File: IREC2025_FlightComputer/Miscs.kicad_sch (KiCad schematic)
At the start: 14 parts, among them U7 THGBMUG6C1LBAIL

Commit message: small fixes
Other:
- moved on the sheet: C73, R49, R50, R51, R52, R53, R54, R55, R56, R57, R58, U7

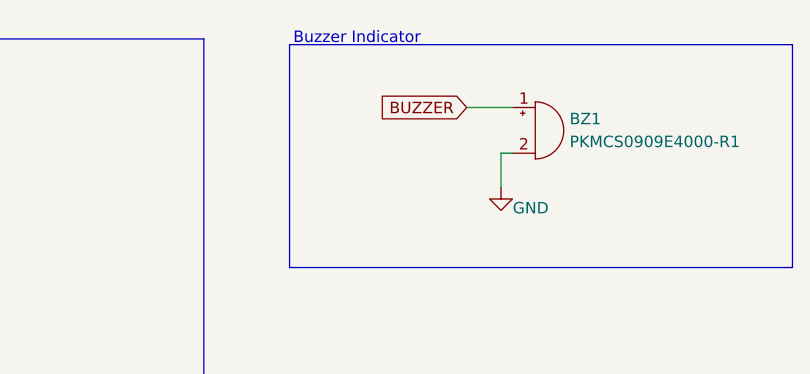
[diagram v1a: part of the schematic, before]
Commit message: Added silkscreen + Layout Minorchange
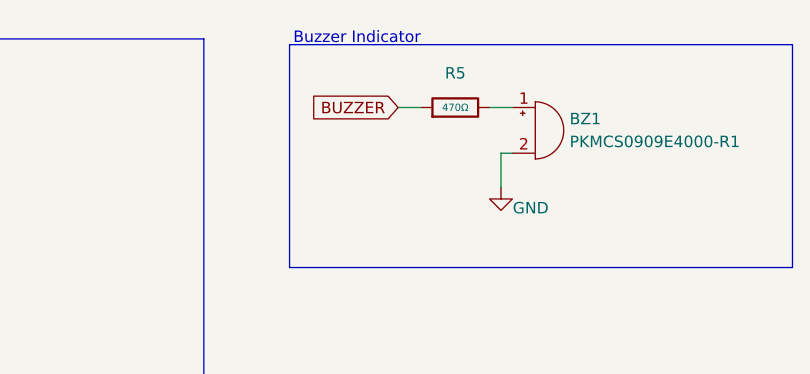
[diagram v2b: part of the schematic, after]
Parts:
- added R5: 470Ω, PCM_JLCPCB:R_0402, symbol PCM_JLCPCB-Resistors:0402,470Ω
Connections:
- net BUZZER: now also R5.1; no longer BZ1.1 (+)
- new net: BZ1.1 (+), R5.2
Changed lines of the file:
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@@
 	(wire
 		(pts
-			(xy 181.61 35.56) (xy 186.69 35.56)
-		)
-		(stroke
-			(width 0)
-			(type default)
-		)
-	)
-	(wire
-		(pts
 			(xy 100.33 209.55) (xy 115.57 209.55)
 		)
@@
 	(wire
 		(pts
+			(xy 173.99 35.56) (xy 176.53 35.56)
+		)
+		(stroke
+			(width 0)
+			(type default)
+		)
+	)
+	(wire
+		(pts
 			(xy 115.57 113.03) (xy 115.57 181.61)
 		)
@@
 	(wire
 		(pts
+			(xy 184.15 35.56) (xy 186.69 35.56)
+		)
+		(stroke
+			(width 0)
+			(type default)
+		)
+	)
+	(wire
+		(pts
 			(xy 111.76 179.07) (xy 111.76 207.01)
 		)
@@
 	(global_label "BUZZER"
 		(shape input)
-		(at 181.61 35.56 180)
+		(at 173.99 35.56 180)
 		(fields_autoplaced yes)
 		(effects
@@
 		)
 		(property "Intersheetrefs" "${INTERSHEET_REFS}"
-			(at 171.1863 35.56 0)
+			(at 163.5663 35.56 0)
 			(effects
 				(font
@@
 					(unit 1)
 				)
+			)
+		)
+	)
+	(symbol
+		(lib_id "PCM_JLCPCB-Resistors:0402,470Ω")
+		(at 180.34 35.56 90)
+		(unit 1)
+		(exclude_from_sim no)
+		(in_bom yes)
+		(on_board yes)
+		(dnp no)
+		(fields_autoplaced yes)
+		(property "Reference" "R5"
+			(at 180.34 31.75 90)
+			(effects
+				(font
+					(size 1.27 1.27)
+				)
+			)
+		)
+		(property "Value" "470Ω"
+			(at 180.34 35.56 90)
+			(do_not_autoplace yes)
+			(effects
+				(font
+					(size 0.8 0.8)
+				)
+			)
+		)
+		(property "Footprint" "PCM_JLCPCB:R_0402"
+			(at 180.34 37.338 90)
+			(effects
+				(font
+					(size 1.27 1.27)
+				)
+				(hide yes)
+			)
+		)
+		(property "Datasheet" "https://www.lcsc.com/datasheet/lcsc_datasheet_2205311900_UNI-ROYAL-Uniroyal-Elec-0402WGF4700TCE_C25117.pdf"
+			(at 180.34 35.56 0)
+			(effects
+				(font
+					(size 1.27 1.27)
+				)
+				(hide yes)
+			)
+		)
+		(property "Description" "62.5mW Thick Film Resistors 50V ±100ppm/°C ±1% 470Ω 0402 Chip Resistor - Surface Mount ROHS"
+			(at 180.34 35.56 0)
+			(effects
+				(font
+					(size 1.27 1.27)
+				)
+				(hide yes)
+			)
+		)
+		(property "LCSC" "C25117"
+			(at 180.34 35.56 0)
+			(effects
+				(font
+					(size 1.27 1.27)
+				)
+				(hide yes)
+			)
+		)
+		(property "Stock" "591787"
+			(at 180.34 35.56 0)
+			(effects
+				(font
+					(size 1.27 1.27)
+				)
+				(hide yes)
+			)
+		)
+		(property "Price" "0.004USD"
+			(at 180.34 35.56 0)
+			(effects
+				(font
+					(size 1.27 1.27)
+				)
+				(hide yes)
+			)
+		)
+		(property "Process" "SMT"
+			(at 180.34 35.56 0)
+			(effects
+				(font
+					(size 1.27 1.27)
+				)
+				(hide yes)
+			)
+		)
+		(property "Minimum Qty" "20"
+			(at 180.34 35.56 0)
+			(effects
+				(font
+					(size 1.27 1.27)
+				)
+				(hide yes)
+			)
+		)
+		(property "Attrition Qty" "10"
+			(at 180.34 35.56 0)
+			(effects
+				(font
+					(size 1.27 1.27)
+				)
+				(hide yes)
+			)
+		)
+		(property "Class" "Basic Component"
+			(at 180.34 35.56 0)
+			(effects
+				(font
+					(size 1.27 1.27)
+				)
+				(hide yes)
+			)
+		)
+		(property "Category" "Resistors,Chip Resistor - Surface Mount"
+			(at 180.34 35.56 0)
+			(effects
+				(font
+					(size 1.27 1.27)
+				)
+				(hide yes)
+			)
+		)
+		(property "Manufacturer" "UNI-ROYAL(Uniroyal Elec)"
+			(at 180.34 35.56 0)
+			(effects
+				(font
+					(size 1.27 1.27)
+				)
+				(hide yes)
+			)
+		)
+		(property "Part" "0402WGF4700TCE"
+			(at 180.34 35.56 0)
+			(effects
+				(font
+					(size 1.27 1.27)
+				)
+				(hide yes)
+			)
+		)
+		(property "Resistance" "470Ω"
+			(at 180.34 35.56 0)
+			(effects
+				(font
+					(size 1.27 1.27)
+				)
+				(hide yes)
+			)
+		)
+		(property "Power(Watts)" "62.5mW"
+			(at 180.34 35.56 0)
+			(effects
+				(font
+					(size 1.27 1.27)
+				)
+				(hide yes)
+			)
+		)
+		(property "Type" "Thick Film Resistors"
+			(at 180.34 35.56 0)
+			(effects
+				(font
+					(size 1.27 1.27)
+				)
+				(hide yes)
+			)
+		)
+		(property "Overload Voltage (Max)" "50V"
+			(at 180.34 35.56 0)
+			(effects
+				(font
+					(size 1.27 1.27)
+				)
+				(hide yes)
+			)
+		)
+		(property "Operating Temperature Range" "-55°C~+155°C"
+			(at 180.34 35.56 0)
+			(effects
+				(font
+					(size 1.27 1.27)
+				)
+				(hide yes)
+			)
+		)
+		(property "Tolerance" "±1%"
+			(at 180.34 35.56 0)
+			(effects
+				(font
+					(size 1.27 1.27)
+				)
+				(hide yes)
+			)
+		)
+		(property "Temperature Coefficient" "±100ppm/°C"
+			(at 180.34 35.56 0)
+			(effects
+				(font
+					(size 1.27 1.27)
+				)
+				(hide yes)
+			)
+		)
+		(pin "1"
+		)
+		(pin "2"
+		)
+		(instances
+			(project ""
+				(path "/d402aac1-6798-4745-a2ce-fc3f8e4c9afb/e5fd5176-e33b-4137-b737-1b6a7c4448a9"
+					(reference "R5")
+					(unit 1)
+				)

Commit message: 2 designs
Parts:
- renumbered BZ1 to BZ?, R5 to R?, U6 to U?
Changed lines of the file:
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@@
 		(dnp no)
 		(fields_autoplaced yes)
-		(property "Reference" "BZ1"
+		(property "Reference" "BZ?"
 			(at 193.04 36.8299 0)
 			(effects
@@
 		)
 		(instances
-			(project ""
+			(project "IREC2025_FlightComputer"
 				(path "/d402aac1-6798-4745-a2ce-fc3f8e4c9afb/e5fd5176-e33b-4137-b737-1b6a7c4448a9"
-					(reference "BZ1")
+					(reference "BZ?")
 					(unit 1)
 				)
@@
 		(dnp no)
 		(fields_autoplaced yes)
-		(property "Reference" "R5"
+		(property "Reference" "R?"
 			(at 180.34 31.75 90)
 			(effects
@@
 		)
 		(instances
-			(project ""
+			(project "IREC2025_FlightComputer"
 				(path "/d402aac1-6798-4745-a2ce-fc3f8e4c9afb/e5fd5176-e33b-4137-b737-1b6a7c4448a9"
-					(reference "R5")
+					(reference "R?")
 					(unit 1)
 				)
@@
 		(dnp no)
 		(fields_autoplaced yes)
-		(property "Reference" "U6"
+		(property "Reference" "U?"
 			(at 204.47 75.5649 0)
 			(effects
@@
 		)
 		(instances
-			(project ""
+			(project "IREC2025_FlightComputer"
 				(path "/d402aac1-6798-4745-a2ce-fc3f8e4c9afb/e5fd5176-e33b-4137-b737-1b6a7c4448a9"
-					(reference "U6")
+					(reference "U?")
 					(unit 1)
 				)

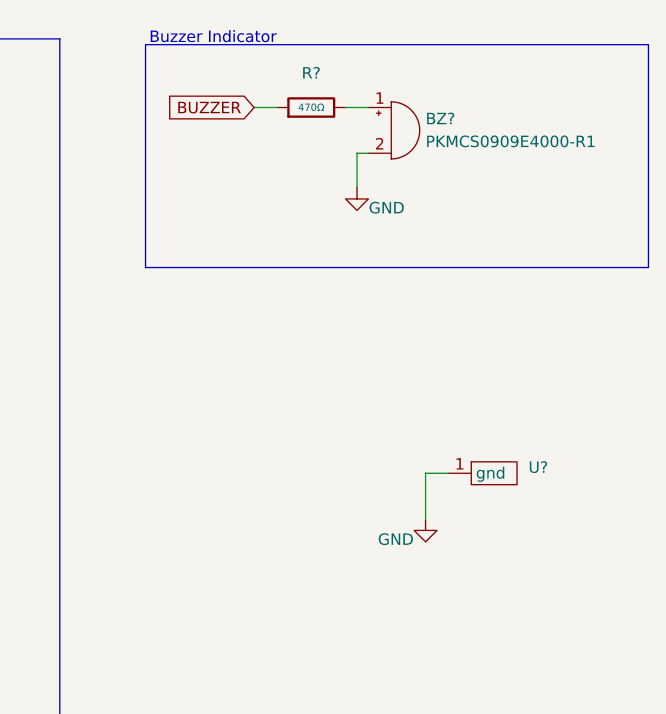
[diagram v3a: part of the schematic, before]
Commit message: changed most resistors to 0603
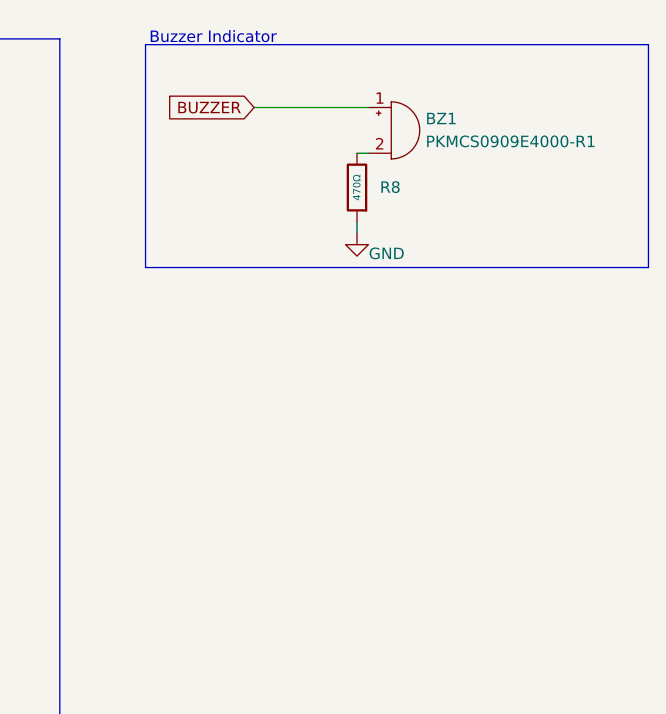
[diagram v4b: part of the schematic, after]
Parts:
- removed U?: ~, RFshielddd:MS233-20, symbol shieldrf:shieldrff
- R8: renamed from R?; footprint PCM_JLCPCB:R_0402 -> PCM_JLCPCB:R_0603
- gave numbers to parts that had none: 1
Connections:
- net BUZZER: now also BZ1.1 (+); no longer R8.1
- net GND: now also R8.1; no longer BZ1.2 (-)
- net at R8.2: now also BZ1.2 (-); no longer BZ1.1 (+)
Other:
- moved on the sheet: R8
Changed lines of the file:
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@@
 	(wire
 		(pts
-			(xy 193.04 81.28) (xy 193.04 76.2)
-		)
-		(stroke
-			(width 0)
-			(type default)
-		)
-	)
-	(wire
-		(pts
 			(xy 72.39 82.55) (xy 72.39 95.25)
 		)
@@
 	(wire
 		(pts
-			(xy 185.42 44.45) (xy 185.42 40.64)
-		)
-		(stroke
-			(width 0)
-			(type default)
-		)
-	)
-	(wire
-		(pts
 			(xy 100.33 209.55) (xy 115.57 209.55)
 		)
@@
 	(wire
 		(pts
-			(xy 193.04 76.2) (xy 195.58 76.2)
-		)
-		(stroke
-			(width 0)
-			(type default)
-		)
-	)
-	(wire
-		(pts
 			(xy 67.31 92.71) (xy 77.47 92.71)
 		)
@@
 	(wire
 		(pts
-			(xy 173.99 35.56) (xy 176.53 35.56)
-		)
-		(stroke
-			(width 0)
-			(type default)
-		)
-	)
-	(wire
-		(pts
 			(xy 115.57 113.03) (xy 115.57 181.61)
 		)
@@
 	(wire
 		(pts
-			(xy 184.15 35.56) (xy 186.69 35.56)
-		)
-		(stroke
-			(width 0)
-			(type default)
-		)
-	)
-	(wire
-		(pts
 			(xy 111.76 179.07) (xy 111.76 207.01)
 		)
@@
 	(wire
 		(pts
+			(xy 185.42 48.26) (xy 185.42 49.53)
+		)
+		(stroke
+			(width 0)
+			(type default)
+		)
+	)
+	(wire
+		(pts
 			(xy 77.47 125.73) (xy 67.31 125.73)
 		)
@@
 	(wire
 		(pts
+			(xy 173.99 35.56) (xy 186.69 35.56)
+		)
+		(stroke
+			(width 0)
+			(type default)
+		)
+	)
+	(wire
+		(pts
 			(xy 100.33 113.03) (xy 115.57 113.03)
 		)
@@
 		(dnp no)
 		(fields_autoplaced yes)
-		(property "Reference" "BZ?"
+		(property "Reference" "BZ1"
 			(at 193.04 36.8299 0)
 			(effects
@@
 			(project "IREC2025_FlightComputer"
 				(path "/d402aac1-6798-4745-a2ce-fc3f8e4c9afb/e5fd5176-e33b-4137-b737-1b6a7c4448a9"
-					(reference "BZ?")
+					(reference "BZ1")
 					(unit 1)
 				)
@@
 	(symbol
 		(lib_id "PCM_JLCPCB-Resistors:0402,470Ω")
-		(at 180.34 35.56 90)
+		(at 185.42 44.45 180)
 		(unit 1)
 		(exclude_from_sim no)
@@
 		(dnp no)
 		(fields_autoplaced yes)
-		(property "Reference" "R?"
-			(at 180.34 31.75 90)
+		(property "Reference" "R8"
+			(at 187.96 44.4499 0)
 			(effects
 				(font
 					(size 1.27 1.27)
 				)
+				(justify right)
 			)
 		)
 		(property "Value" "470Ω"
-			(at 180.34 35.56 90)
+			(at 185.42 44.45 90)
 			(do_not_autoplace yes)
 			(effects
@@
 			)
 		)
-		(property "Footprint" "PCM_JLCPCB:R_0402"
-			(at 180.34 37.338 90)
+		(property "Footprint" "PCM_JLCPCB:R_0603"
+			(at 187.198 44.45 90)
 			(effects
 				(font
@@
 		)
 		(property "Datasheet" "https://www.lcsc.com/datasheet/lcsc_datasheet_2205311900_UNI-ROYAL-Uniroyal-Elec-0402WGF4700TCE_C25117.pdf"
-			(at 180.34 35.56 0)
+			(at 185.42 44.45 0)
 			(effects
 				(font
@@
 		)
 		(property "Description" "62.5mW Thick Film Resistors 50V ±100ppm/°C ±1% 470Ω 0402 Chip Resistor - Surface Mount ROHS"
-			(at 180.34 35.56 0)
+			(at 185.42 44.45 0)
 			(effects
 				(font
@@
 		)
 		(property "LCSC" "C25117"
-			(at 180.34 35.56 0)
+			(at 185.42 44.45 0)
 			(effects
 				(font
@@
 		)
 		(property "Stock" "591787"
-			(at 180.34 35.56 0)
+			(at 185.42 44.45 0)
 			(effects
 				(font
@@
 		)
 		(property "Price" "0.004USD"
-			(at 180.34 35.56 0)
+			(at 185.42 44.45 0)
 			(effects
 				(font
@@
 		)
 		(property "Process" "SMT"
-			(at 180.34 35.56 0)
+			(at 185.42 44.45 0)
 			(effects
 				(font
@@
 		)
 		(property "Minimum Qty" "20"
-			(at 180.34 35.56 0)
+			(at 185.42 44.45 0)
 			(effects
 				(font
@@
 		)
 		(property "Attrition Qty" "10"
-			(at 180.34 35.56 0)
+			(at 185.42 44.45 0)
 			(effects
 				(font
@@
 		)
 		(property "Class" "Basic Component"
-			(at 180.34 35.56 0)
+			(at 185.42 44.45 0)
 			(effects
 				(font
@@
 		)
 		(property "Category" "Resistors,Chip Resistor - Surface Mount"
-			(at 180.34 35.56 0)
+			(at 185.42 44.45 0)
 			(effects
 				(font
@@
 		)
 		(property "Manufacturer" "UNI-ROYAL(Uniroyal Elec)"
-			(at 180.34 35.56 0)
+			(at 185.42 44.45 0)
 			(effects
 				(font
@@
 		)
 		(property "Part" "0402WGF4700TCE"
-			(at 180.34 35.56 0)
+			(at 185.42 44.45 0)
 			(effects
 				(font
@@
 		)
 		(property "Resistance" "470Ω"
-			(at 180.34 35.56 0)
+			(at 185.42 44.45 0)
 			(effects
 				(font
@@
 		)
 		(property "Power(Watts)" "62.5mW"
-			(at 180.34 35.56 0)
+			(at 185.42 44.45 0)
 			(effects
 				(font
@@
 		)
 		(property "Type" "Thick Film Resistors"
-			(at 180.34 35.56 0)
+			(at 185.42 44.45 0)
 			(effects
 				(font
@@
 		)
 		(property "Overload Voltage (Max)" "50V"
-			(at 180.34 35.56 0)
+			(at 185.42 44.45 0)
 			(effects
 				(font
@@
 		)
 		(property "Operating Temperature Range" "-55°C~+155°C"
-			(at 180.34 35.56 0)
+			(at 185.42 44.45 0)
 			(effects
 				(font
@@
 		)
 		(property "Tolerance" "±1%"
-			(at 180.34 35.56 0)
+			(at 185.42 44.45 0)
 			(effects
 				(font
@@
 		)
 		(property "Temperature Coefficient" "±100ppm/°C"
-			(at 180.34 35.56 0)
+			(at 185.42 44.45 0)
 			(effects
 				(font
@@
 			(project "IREC2025_FlightComputer"
 				(path "/d402aac1-6798-4745-a2ce-fc3f8e4c9afb/e5fd5176-e33b-4137-b737-1b6a7c4448a9"
-					(reference "R?")
+					(reference "R8")
 					(unit 1)
 				)
@@
 	(symbol
 		(lib_id "power:GND")
-		(at 193.04 81.28 0)
-		(unit 1)
-		(exclude_from_sim no)
-		(in_bom yes)
-		(on_board yes)
-		(dnp no)
-		(property "Reference" "#PWR0118"
-			(at 193.04 87.63 0)
-			(effects
-				(font
-					(size 1.27 1.27)
-				)
-				(hide yes)
-			)
-		)
-		(property "Value" "GND"
-			(at 189.738 83.566 0)
-			(effects
-				(font
-					(size 1.27 1.27)
-				)
-			)
-		)
-		(property "Footprint" ""
-			(at 193.04 81.28 0)
-			(effects
-				(font
-					(size 1.27 1.27)
-				)
-				(hide yes)
-			)
-		)
-		(property "Datasheet" ""
-			(at 193.04 81.28 0)
-			(effects
-				(font
-					(size 1.27 1.27)
-				)
-				(hide yes)
-			)
-		)
-		(property "Description" "Power symbol creates a global label with name \"GND\" , ground"
-			(at 193.04 81.28 0)
-			(effects
-				(font
-					(size 1.27 1.27)
-				)
-				(hide yes)
-			)
-		)
-		(pin "1"
-		)
-		(instances
-			(project "IREC2025_FlightComputer"
-				(path "/d402aac1-6798-4745-a2ce-fc3f8e4c9afb/e5fd5176-e33b-4137-b737-1b6a7c4448a9"
-					(reference "#PWR0118")
-					(unit 1)
-				)
-			)
-		)
-	)
-	(symbol
-		(lib_id "power:GND")
-		(at 185.42 44.45 0)
+		(at 185.42 49.53 0)
 		(mirror y)
 		(unit 1)
@@
 		(dnp no)
 		(property "Reference" "#PWR0117"
-			(at 185.42 50.8 0)
+			(at 185.42 55.88 0)
 			(effects
 				(font
@@
 		)
 		(property "Value" "GND"
-			(at 188.722 46.736 0)
+			(at 188.722 51.816 0)
 			(effects
 				(font
@@
 		)
 		(property "Footprint" ""
-			(at 185.42 44.45 0)
+			(at 185.42 49.53 0)
 			(effects
 				(font
@@
 		)
 		(property "Datasheet" ""
-			(at 185.42 44.45 0)
+			(at 185.42 49.53 0)
 			(effects
 				(font
@@
 		)
 		(property "Description" "Power symbol creates a global label with name \"GND\" , ground"
-			(at 185.42 44.45 0)
+			(at 185.42 49.53 0)
 			(effects
 				(font
@@
 					(unit 1)
 				)
-			)
-		)
-	)
-	(symbol
-		(lib_id "shieldrf:shieldrff")
-		(at 200.66 77.47 0)
-		(unit 1)
-		(exclude_from_sim no)
-		(in_bom yes)
-		(on_board yes)
-		(dnp no)
-		(fields_autoplaced yes)
-		(property "Reference" "U?"
-			(at 204.47 75.5649 0)
-			(effects
-				(font
-					(size 1.27 1.27)
-				)
-				(justify left)
-			)
-		)
-		(property "Value" "~"
-			(at 204.47 77.47 0)
-			(effects
-				(font
-					(size 1.27 1.27)
-				)
-				(justify left)
-			)
-		)
-		(property "Footprint" "RFshielddd:MS233-20"
-			(at 200.66 77.47 0)
-			(effects
-				(font
-					(size 1.27 1.27)
-				)
-				(hide yes)
-			)
-		)
-		(property "Datasheet" ""
-			(at 200.66 77.47 0)
-			(effects
-				(font
-					(size 1.27 1.27)
-				)
-				(hide yes)
-			)
-		)
-		(property "Description" ""
-			(at 200.66 77.47 0)
-			(effects
-				(font
-					(size 1.27 1.27)
-				)
-				(hide yes)
-			)
-		)
-		(pin "1"
-		)
-		(instances
-			(project "IREC2025_FlightComputer"
-				(path "/d402aac1-6798-4745-a2ce-fc3f8e4c9afb/e5fd5176-e33b-4137-b737-1b6a7c4448a9"
-					(reference "U?")
-					(unit 1)
-				)
